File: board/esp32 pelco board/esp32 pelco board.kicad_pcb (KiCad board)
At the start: 2 copper layers, 213.4 x 88.7 mm, 71 parts, among them J1 Conn_02x05_Odd_Even, J10 qwiic, J11 Conn_01x02, J12 from connector, J13 battery bypass, J14 to rest of device, J15 qwiic, J16 qwiic, J2 Conn_02x03_Odd_Even, J3 qwiic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

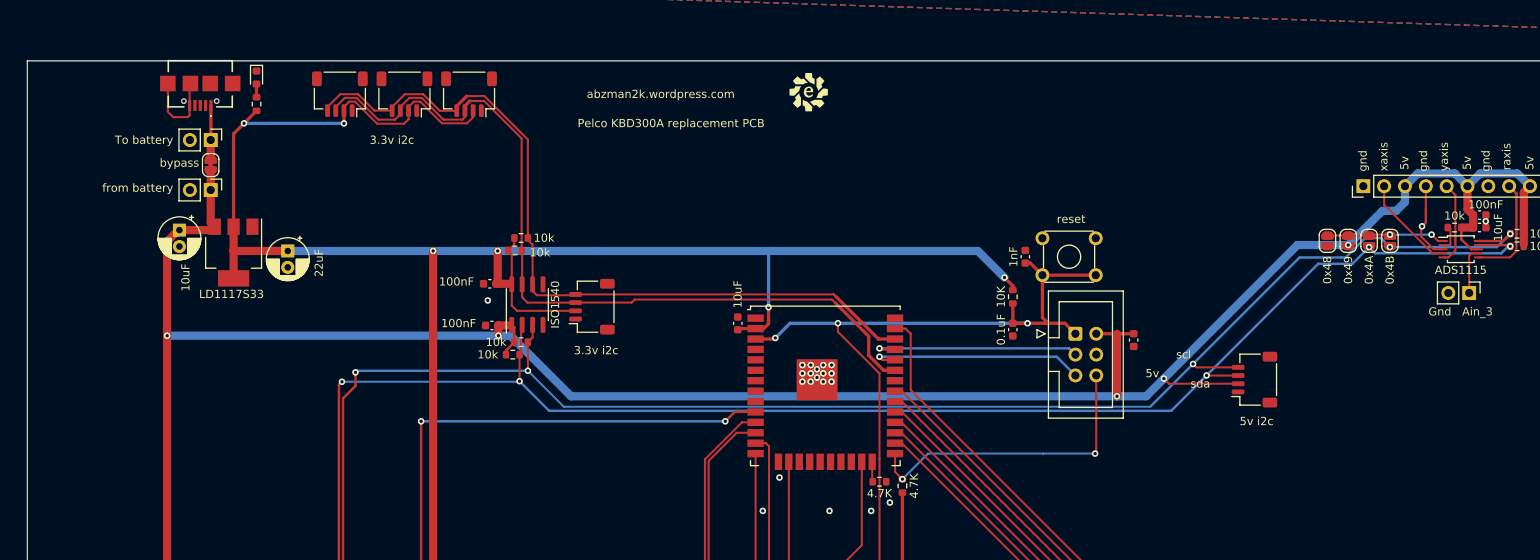
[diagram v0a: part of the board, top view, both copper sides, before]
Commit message: added usb serial and programming button
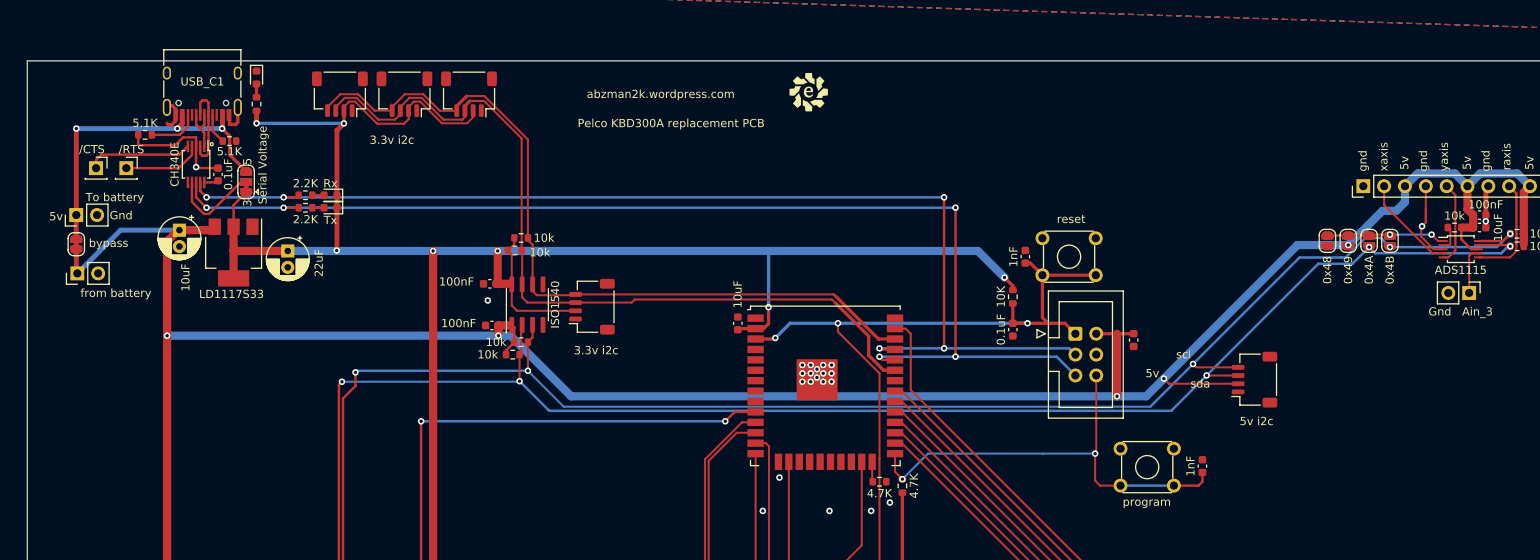
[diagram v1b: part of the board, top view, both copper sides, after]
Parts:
- added C13: 0.1uF, Capacitor_SMD:C_0603_1608Metric, F.Cu at (23.2, 13.8)
- added C14: 1nF, Capacitor_SMD:C_0603_1608Metric, F.Cu at (143.3, 49.4)
- added D2: Tx, LED_SMD:LED_0603_1608Metric, F.Cu at (37.0, 17.9)
- added D3: Rx, LED_SMD:LED_0603_1608Metric, F.Cu at (37.0, 16.4)
- added J17: /RTS, Connector_PinSocket_2.54mm:PinSocket_1x01_P2.54mm_Vertical, F.Cu at (12.1, 13.1)
- added JP11: Serial Voltage, Jumper:SolderJumper-3_P1.3mm_Bridged12_RoundedPad1.0x1.5mm, F.Cu at (26.7, 14.8)
- added R24: 5.1K, Resistor_SMD:R_0603_1608Metric, F.Cu at (24.6, 9.78)
- added R25: 5.1K, Resistor_SMD:R_0603_1608Metric, F.Cu at (14.4, 9.02)
- added R26: 2.2K, Resistor_SMD:R_0603_1608Metric, F.Cu at (33.9, 17.9)
- added R27: 2.2K, Resistor_SMD:R_0603_1608Metric, F.Cu at (33.9, 16.4)
- added SW2: program, Button_Switch_THT:SW_TH_Tactile_Omron_B3F-10xx, F.Cu at (133.3, 47.3)
- added U3: CH340E, Package_SO:MSOP-10_3x3mm_P0.5mm, F.Cu at (20.6, 12.6)
- added USB_C1: TYPE-C-31-M-12, Connector_USB:USB_C_Receptacle_HRO_TYPE-C-31-M-12, F.Cu at (21.3, 2.54)
- J6: value UJ2-MIBH-G-SMT-TR -> /CTS; footprint Evan's misc parts:UJ2MIBHGSMTTR -> Connector_PinSocket_2.54mm:PinSocket_1x01_P2.54mm_Vertical
- SW1: value SW_MEC_5E -> reset
- moved J14 19.2 mm to (6.10, 25.9), turned to 90 degrees
- moved J13 19.0 mm to (5.97, 22.4)
- moved J12 18.8 mm to (5.96, 18.8), turned to 90 degrees
- moved J6 16.3 mm to (8.38, 13.1), turned to 0 degrees
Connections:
- J6 pad 1: VCC -> Net-(J6-Pin_1)
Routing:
- net /ESP_IO3: track 26.9 -> 141.8 mm, vias 1 -> 5
- net /ESP_IO1: track 26.1 -> 138.6 mm, vias 1 -> 5
- net VCC: track 6.63 -> 41.3 mm, vias 0 -> 3
- net /ESP_IO0: track 37.9 -> 55.8 mm
- net GND: track 33.2 -> 49.7 mm, vias 29 -> 30
- net Net-(J6-Pin_1): track 0.00 -> 12.9 mm
- net Net-(JP11-C): track 0.00 -> 11.2 mm
- net D-: track 0.00 -> 11.0 mm
- net +5V: track 385.4 -> 395.2 mm
- net Net-(J17-Pin_1): track 0.00 -> 9.73 mm
- net Net-(USB_C1-CC2): track 0.00 -> 6.26 mm
- net D+: track 0.00 -> 6.19 mm
- net +3V3: track 311.7 -> 317.0 mm, vias 8 -> 9
- net Net-(USB_C1-CC1): track 0.00 -> 3.70 mm
- net Net-(U3-V3): track 0.00 -> 1.75 mm
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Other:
- board text added: "3"

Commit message: updated gitignore and board tweaks
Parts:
- added REF**: MountingHole_3.2mm_M3, MountingHole:MountingHole_3.2mm_M3, F.Cu at (205.7, 76.2)
- added REF**: MountingHole_3.2mm_M3, MountingHole:MountingHole_3.2mm_M3, F.Cu at (152.4, 76.2)
- added REF**: MountingHole_3.2mm_M3, MountingHole:MountingHole_3.2mm_M3, F.Cu at (205.7, 50.8)
- added REF**: MountingHole_3.2mm_M3, MountingHole:MountingHole_3.2mm_M3, F.Cu at (5.08, 50.8)
- added REF**: MountingHole_3.2mm_M3, MountingHole:MountingHole_3.2mm_M3, F.Cu at (33.0, 50.8)
- added REF**: MountingHole_3.2mm_M3, MountingHole:MountingHole_3.2mm_M3, F.Cu at (152.4, 50.8)
- added REF**: MountingHole_3.2mm_M3, MountingHole:MountingHole_3.2mm_M3, F.Cu at (55.9, 50.8)
- added REF**: MountingHole_3.2mm_M3, MountingHole:MountingHole_3.2mm_M3, F.Cu at (76.2, 50.8)
- moved R27 29.2 mm to (8.89, 1.27)
- moved R26 29.0 mm to (8.89, 3.17)
- moved D3 27.2 mm to (14.4, 1.27)
- moved D2 27.0 mm to (14.4, 3.17)
- moved R25 3.96 mm to (14.0, 5.08)
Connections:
- J10 pad MP: (no net) -> GND
- J15 pad MP: (no net) -> GND
- J16 pad MP: (no net) -> GND
- J3 pad MP: (no net) -> GND
- J7 pad 4: unconnected-(J7-Pin_4-Pad4) -> +5V
- J7 pad 5: unconnected-(J7-Pin_5-Pad5) -> +5V
- J8 pad MP: (no net) -> GND
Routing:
- net /ESP_IO1: track 138.6 -> 170.9 mm
- net /ESP_IO3: track 141.8 -> 173.4 mm
- net +5V: track 395.2 -> 415.2 mm, vias 7 -> 8
- net +3V3: track 317.0 -> 335.8 mm
- net GND: track 49.7 -> 52.1 mm, vias 30 -> 73
- net Net-(D3-A): track 1.44 -> 3.47 mm
- net Net-(D2-A): track 1.44 -> 3.47 mm
- net Net-(USB_C1-CC2): track 6.26 -> 7.78 mm
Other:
- board text added: "These resistors mess with the keypad, only populate them if you're not using these oins for the keypad"

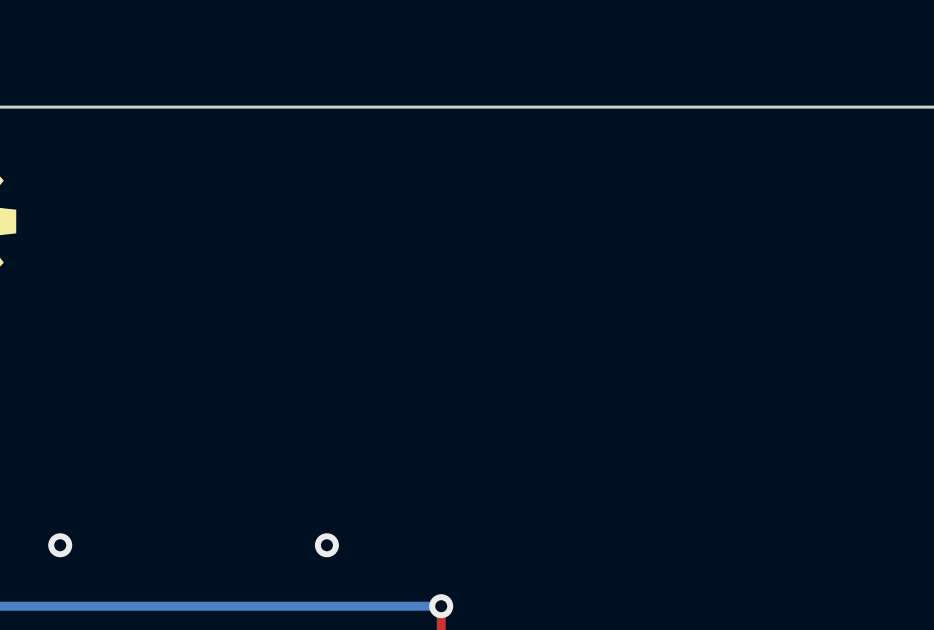
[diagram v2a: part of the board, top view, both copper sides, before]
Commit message: added pcbway logo
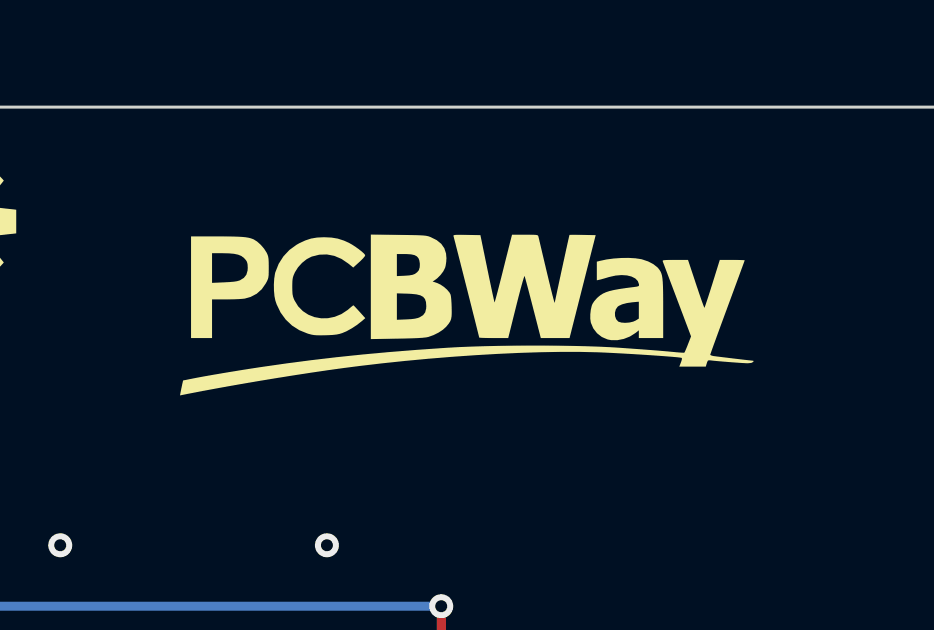
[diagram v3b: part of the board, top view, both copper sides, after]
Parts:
- added G***: LOGO, Evan's parts:pcbway logo, F.Cu at (112.5, 6.86)

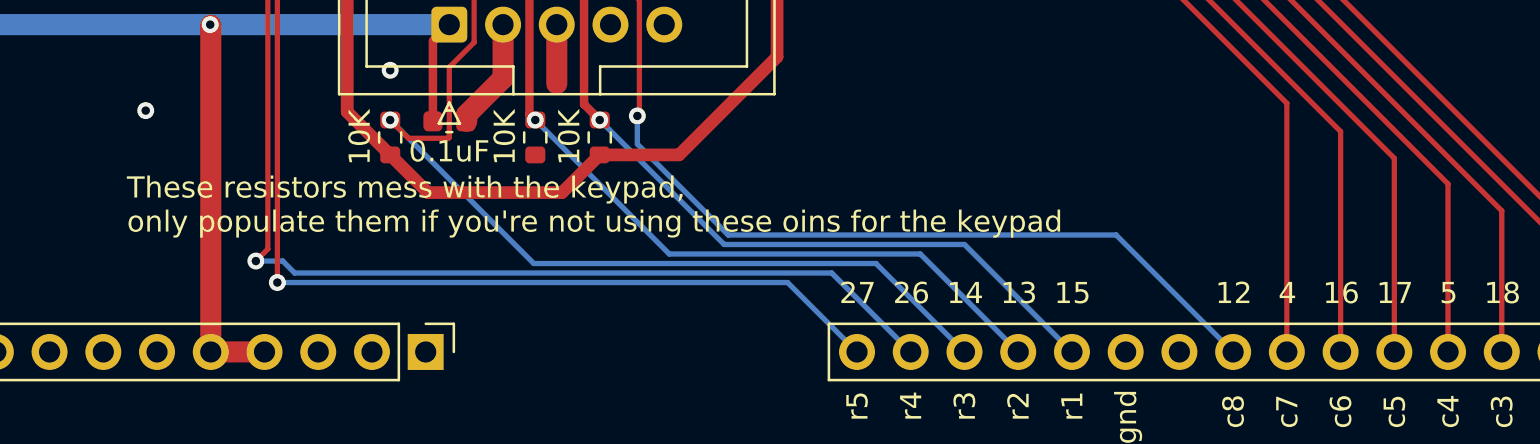
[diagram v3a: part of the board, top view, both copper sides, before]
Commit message: tweaks to silk and new gerbers
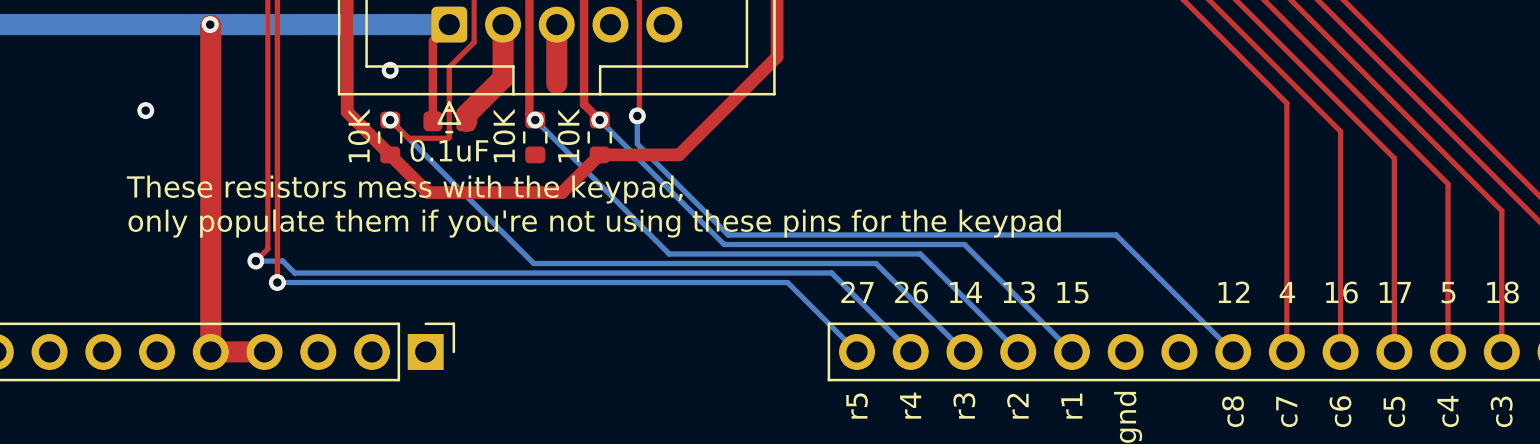
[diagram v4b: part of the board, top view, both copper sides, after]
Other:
- board text added: "These resistors mess with the keypad, only populate them if you're not using these pins for the keypad"
- board text removed: "These resistors mess with the keypad, only populate them if you're not using these oins for the keypad"
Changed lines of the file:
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@@
     (effects (font (size 1 1) (thickness 0.15)))
   )
-  (gr_text "These resistors mess with the keypad, \nonly populate them if you're not using these oins for the keypad" (at 75.946 76.962) (layer "F.SilkS")
+  (gr_text "These resistors mess with the keypad, \nonly populate them if you're not using these pins for the keypad" (at 75.946 76.962) (layer "F.SilkS")
     (effects (font (size 1 1) (thickness 0.15)) (justify left bottom))
   )

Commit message: added silk assembly note
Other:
- board text added: "you MUST solder one (I say must, it might always come up as 0x49, but how sure are you that will always be the case?)"
